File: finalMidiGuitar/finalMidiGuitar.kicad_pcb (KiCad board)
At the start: 2 copper layers, 71 x 35.1 mm, 36 parts, among them J1 PinHeader_01x06_P2.54mm_Verti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, J2 PinHeader_01x06_P2.54mm_Verti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, J3 NeoPixel, J4 Oled Display, M1 Module_XIAO_Generic_SocketSMD, SW1 BTN, U1 SN74LVC1T45DBVR

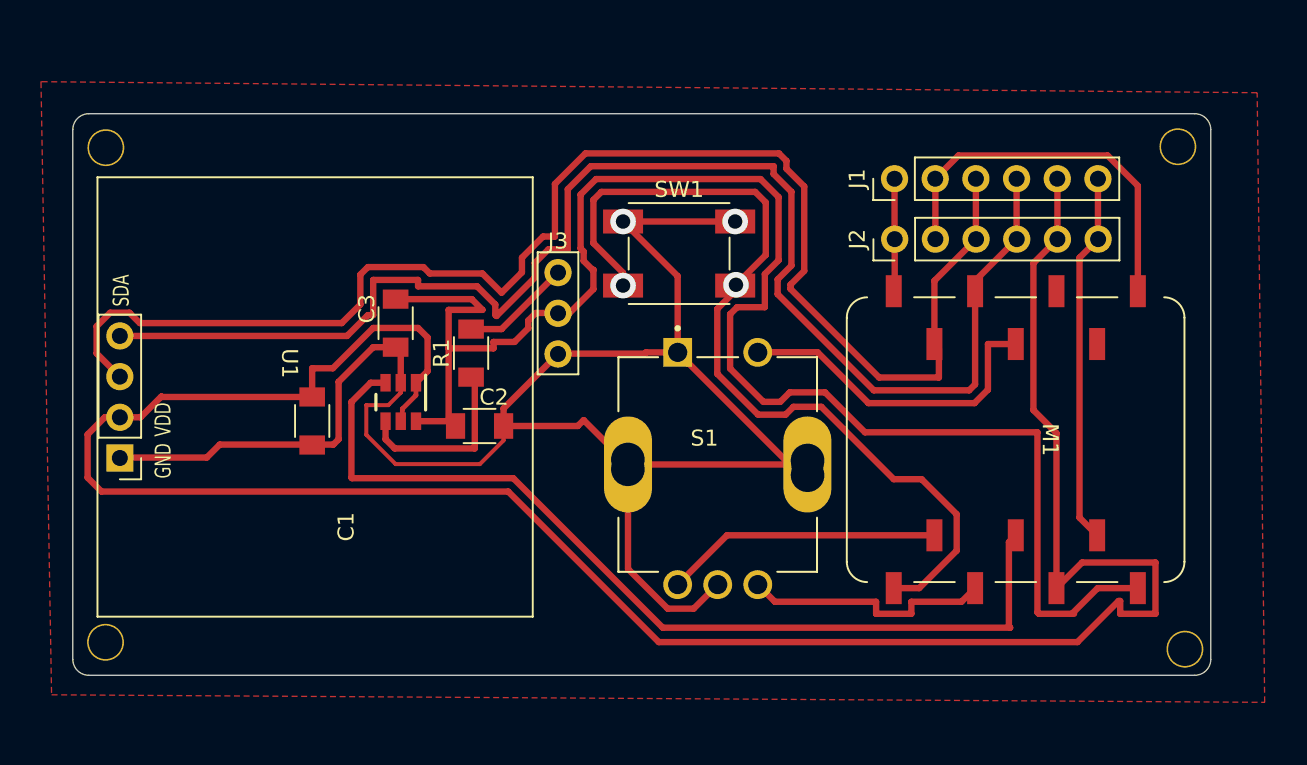
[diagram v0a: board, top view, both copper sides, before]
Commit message: Add sensor interrupt handling and enhance button functionality for context-sensitive actions
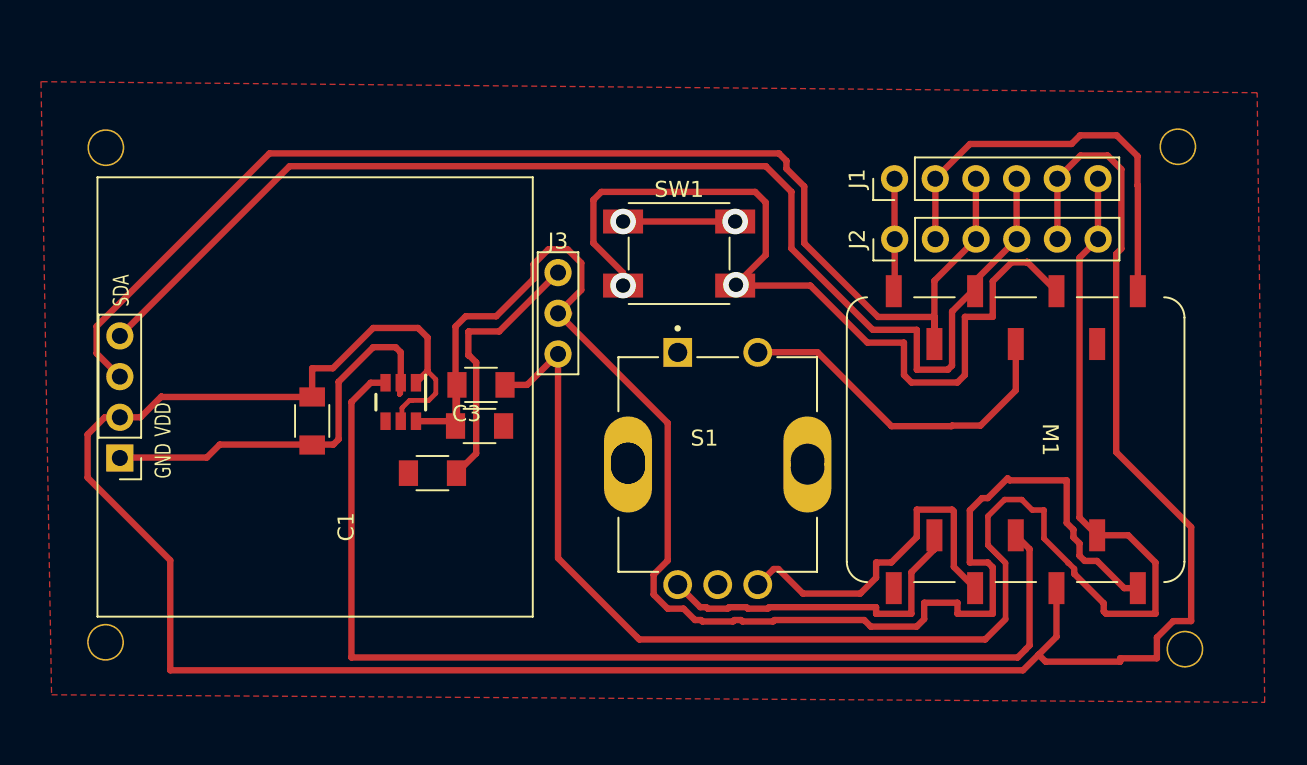
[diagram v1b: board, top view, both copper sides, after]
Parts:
- removed the ? at (163.9, 130.5)
- removed the ? at (152.7, 130.1)
- removed the ? at (152.7, 129.5)
- removed the REF** at (121.3, 114.4)
- removed the REF** at (121.6, 115.0)
- removed the REF** at (144.4, 136.7)
- removed the REF** at (144.7, 114.9)
- removed the REF** at (121.6, 137.3)
- removed the REF** at (144.7, 137.3)
- removed the REF** at (144.4, 114.4)
- removed the REF** at (144.7, 113.9)
- removed the REF** at (121.3, 136.8)
- removed the REF** at (121.6, 136.2)
- removed the REF** at (121.9, 114.4)
- removed the REF** at (144.7, 136.2)
- removed the REF** at (145.0, 136.8)
- removed the REF** at (121.9, 136.8)
- removed the REF** at (145.0, 114.4)
- removed the REF** at (121.6, 113.9)
- added ? (x2): , , F.Cu at (121.6, 137.0)
- added ? (x2): , , F.Cu at (121.6, 136.5)
- added ? (x2): , , F.Cu at (144.7, 136.5)
- added ? (x2): , , F.Cu at (152.7, 130.0)
- added ? (x2): , , F.Cu at (144.7, 137.0)
- added ? (x2): , , F.Cu at (121.6, 114.1)
- added ? (x2): , , F.Cu at (144.7, 114.1)
- added ? (x2): , , F.Cu at (121.6, 114.6)
- added ? (x2): , , F.Cu at (144.7, 114.5)
- added ? (x2): , , F.Cu at (152.7, 129.5)
- added ?: , , F.Cu at (163.9, 130.0)
- moved R1 7.87 mm to (140.5, 130.3), turned to 0 degrees
- moved C3 6.58 mm to (143.5, 124.8), turned to 180 degrees
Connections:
- M1 pad 3: unconnected-(M1-D2-Pad3) -> Net-(M1-D2)
- M1 pad 8: Net-(M1-D7) -> unconnected-(M1-D7-Pad8)
- SW1 pad 2: Net-(M1-D7) -> Net-(M1-D2)
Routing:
- net Net-(M1-D7): track 55.5 -> 0.00 mm, vias 2 -> 0
- net Net-(M1-D2): track 0.00 -> 54.4 mm, vias 0 -> 2
- net PWR_3V3: track 143.9 -> 160.5 mm
- net Net-(U1-B): track 11.5 -> 0.00 mm
- net SDA: track 89.4 -> 78.7 mm
- net SCL: track 90.9 -> 80.2 mm
- net Net-(J3-Pin_1): track 6.40 -> 16.7 mm
- net Net-(M1-D10): track 58.3 -> 68.5 mm
- net Net-(M1-D9): track 15.9 -> 22.4 mm
- net PWR_5V: track 101.1 -> 96.2 mm
- net Net-(M1-D8): track 17.3 -> 21.2 mm
- net PWR_GND: track 138.4 -> 135.7 mm
- net INT: track 24.4 -> 26.5 mm
- net Net-(M1-D3): track 20.6 -> 21.8 mm
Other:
- board outline removed

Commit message: Update pad dimensions and clean up schematic and pcb
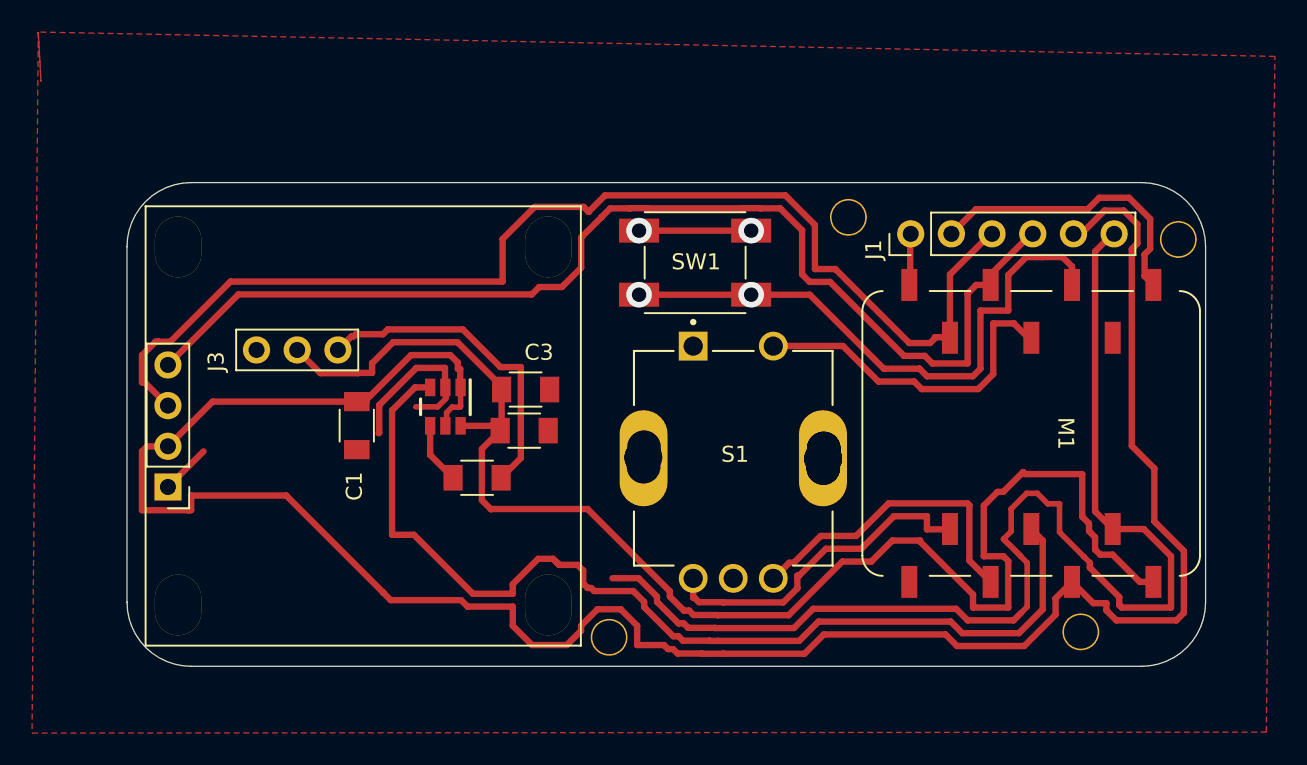
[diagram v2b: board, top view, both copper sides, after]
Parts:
- removed the ? at (121.6, 137.0) (x2)
- removed the ? at (121.6, 136.5) (x2)
- removed the ? at (144.7, 136.5) (x2)
- removed the ? at (152.7, 130.0) (x2)
- removed the ? at (144.7, 137.0) (x2)
- removed the ? at (121.6, 114.1) (x2)
- removed the ? at (144.7, 114.1) (x2)
- removed the ? at (121.6, 114.6) (x2)
- removed the ? at (144.7, 114.5) (x2)
- removed the ? at (152.7, 129.5) (x2)
- removed the ? at (163.9, 129.6)
- removed the ? at (163.9, 130.0)
- removed J2: PinHeader_01x06_P2.54mm_Vertical_THT_D1mm, PCM_fab:PinHeader_01x06_P2.54mm_Vertical_THT_D1mm
- removed the REF** at (187.0, 110.0)
- added ? (x2): , , F.Cu at (164.9, 130.0)
- added ?: , , F.Cu at (153.8, 129.4)
- added ? (x2): , , F.Cu at (165.0, 129.4)
- added ? (x2): , , F.Cu at (147.6, 116.2)
- added ? (x2): , , F.Cu at (124.4, 116.8)
- added ? (x2): , , F.Cu at (164.8, 129.4)
- added ? (x2): , , F.Cu at (147.5, 139.1)
- added ?: , , F.Cu at (147.6, 116.5)
- added ?: , , F.Cu at (153.7, 129.9)
- added ?: , , F.Cu at (124.4, 116.2)
- added ? (x2): , , F.Cu at (153.5, 129.4)
- added ?: , , F.Cu at (164.9, 128.8)
- added ?: , , F.Cu at (147.5, 138.5)
- added REF**: MountingHole_M2, PCM_fab:MountingHole_M2, F.Cu at (166.5, 114.4)
- added REF**: MountingHole_M2, PCM_fab:MountingHole_M2, F.Cu at (153.7, 128.7)
- added REF**: MountingHole_M2, PCM_fab:MountingHole_M2, F.Cu at (124.4, 115.6)
- added REF**: MountingHole_M2, PCM_fab:MountingHole_M2, F.Cu at (187.1, 115.8)
- added REF**: MountingHole_M2, PCM_fab:MountingHole_M2, F.Cu at (147.6, 115.9)
- added REF**: MountingHole_M2, PCM_fab:MountingHole_M2, F.Cu at (164.9, 128.8)
- added REF**: MountingHole_M2, PCM_fab:MountingHole_M2, F.Cu at (147.6, 137.9)
- moved REF** 43.8 mm to (151.5, 140.6)
- moved REF** 37.2 mm to (147.7, 116.0)
- moved J3 14.6 mm to (134.6, 122.7), turned to -90 degrees
- moved REF** 6.59 mm to (181.0, 140.3)
- moved J1 3.59 mm to (170.4, 115.4)
- moved J4 3.51 mm to (124.0, 127.4)
- moved U1 2.80 mm to (141.3, 126.2)
- moved C1 2.80 mm to (135.8, 127.4)
- moved C2 2.80 mm to (146.2, 127.7)
- moved C3 2.80 mm to (146.3, 125.1)
- moved R1 2.80 mm to (143.3, 130.6)
- moved SW1 1.15 mm to (156.9, 117.2)
- moved S1 1.05 mm to (159.3, 129.4)
- moved M1 1.05 mm to (177.9, 127.9)
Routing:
- net PWR_GND: track 135.7 -> 101.5 mm
- net PWR_3V3: track 160.5 -> 140.0 mm
- net Net-(M1-D2): track 54.4 -> 37.0 mm
- net INT: track 26.5 -> 18.4 mm
- net SDA: track 78.7 -> 71.4 mm
- net SCL: track 80.2 -> 73.7 mm
- net PWR_5V: track 96.2 -> 91.0 mm
- net Net-(M1-D10): track 68.5 -> 64.0 mm
- net Net-(U1-B): track 0.00 -> 3.83 mm
- net XSHUT: track 7.05 -> 3.29 mm
- net Net-(J3-Pin_1): track 16.7 -> 20.3 mm
- net Net-(M1-D9): track 22.4 -> 19.6 mm
- net (no net): track 1.66 -> 0.00 mm
- net Net-(M1-D3): track 21.8 -> 21.2 mm
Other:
- board outline added: 67.3 x 30.2 mm

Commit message: Remove lock files for KiCad PCB and schematic
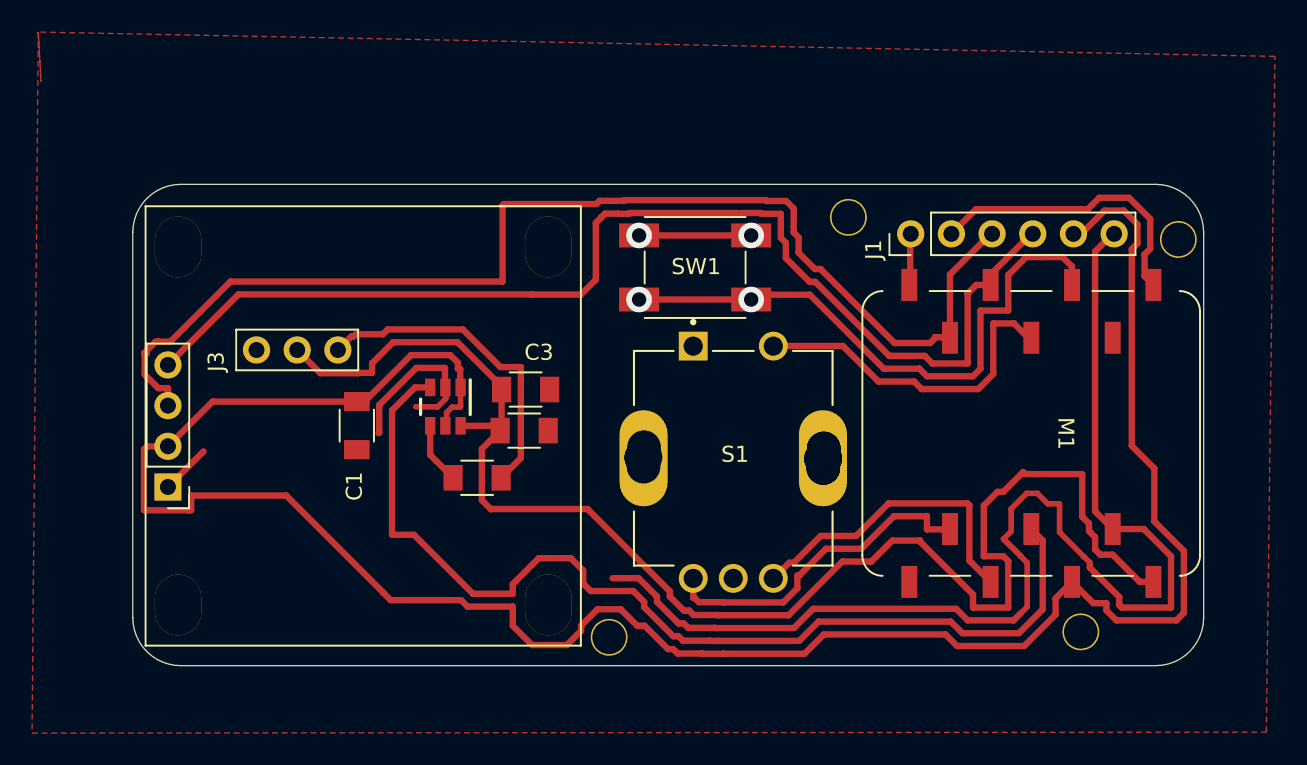
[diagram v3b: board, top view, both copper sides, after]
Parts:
- removed the ? at (147.6, 116.2) (x2)
- removed the ? at (147.6, 116.5)
- removed the REF** at (147.6, 115.9)
- removed the REF** at (147.7, 116.0)
- added ?: , , F.Cu at (124.6, 138.6)
- added ? (x4): , , F.Cu at (147.7, 116.8)
- added ? (x4): , , F.Cu at (124.6, 139.2)
- added ?: , , F.Cu at (147.8, 115.6)
- added ? (x2): , , F.Cu at (147.8, 116.2)
- added REF**: MountingHole_M2, PCM_fab:MountingHole_M2, F.Cu at (147.8, 115.6)
- added REF**: MountingHole_M2, PCM_fab:MountingHole_M2, F.Cu at (124.6, 137.9)
- moved SW1 0.30 mm to (156.9, 117.5)
- moved ? 0.20 mm to (124.6, 116.9) (x2)
- moved REF** 0.20 mm to (124.6, 115.6)
- moved ? 0.20 mm to (124.6, 116.2)
- moved ? 0.19 mm to (147.7, 139.2) (x2)
- moved REF** 0.19 mm to (147.7, 137.9)
- moved ? 0.19 mm to (147.7, 138.6)
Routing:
- net PWR_3V3: track 140.0 -> 139.1 mm
- net SCL: track 73.7 -> 74.5 mm
- net SDA: track 71.4 -> 72.0 mm
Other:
- board size 67.3 x 30.2 mm -> 66.9 x 30.1 mm

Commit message: Add new CAD and backup files for Midi Guitar project
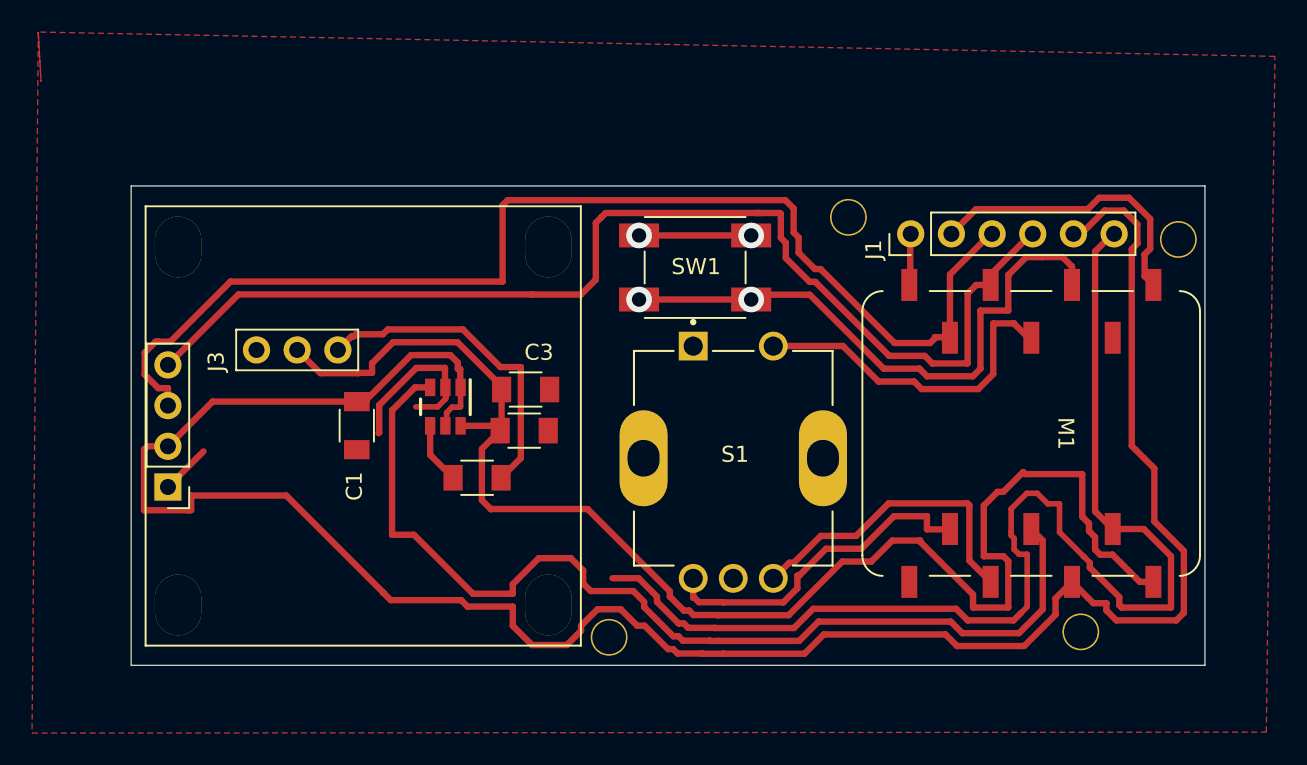
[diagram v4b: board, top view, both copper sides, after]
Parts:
- removed ? (x29): , 
- removed the REF** at (147.8, 115.6)
- removed the REF** at (153.7, 128.7)
- removed the REF** at (124.6, 137.9)
- removed the REF** at (124.6, 115.6)
- removed the REF** at (164.9, 128.8)
- removed the REF** at (147.7, 137.9)
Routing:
- net PWR_GND: track 101.5 -> 99.9 mm
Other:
- board size 66.9 x 30.1 mm -> 67 x 29.9 mm
